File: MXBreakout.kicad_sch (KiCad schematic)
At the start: 16 parts, among them U1 Wii-MX, X1 32.768kHz

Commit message: initial changes
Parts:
- removed TP4: DATA0, TestPoint:TestPoint_Pad_D1.0mm, symbol Connector:TestPoint
- removed TP5: DATA1, TestPoint:TestPoint_Pad_D1.0mm, symbol Connector:TestPoint
- removed TP6: DATA2, TestPoint:TestPoint_Pad_D1.0mm, symbol Connector:TestPoint
- removed TP7: DATA3, TestPoint:TestPoint_Pad_D1.0mm, symbol Connector:TestPoint
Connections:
- net DATA3: now reaches U1.14 (DATA3)
- net DATA1: now reaches U1.12 (DATA1)
- net DATA2: now reaches U1.13 (DATA2)
- net DATA0: now reaches U1.11 (DATA0)
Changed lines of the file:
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@@
-    (stroke (width 0) (type default))
-  )
-  (wire (pts (xy 93.98 85.09) (xy 93.98 88.9))
     (stroke (width 0) (type default))
   )
@@
     (stroke (width 0) (type default))
   )
-  (wire (pts (xy 93.98 96.52) (xy 87.63 96.52))
-    (stroke (width 0) (type default))
-  )
-  (wire (pts (xy 93.98 90.17) (xy 93.98 91.44))
+  (wire (pts (xy 87.63 96.52) (xy 96.52 96.52))
     (stroke (width 0) (type default))
   )
@@
     (stroke (width 0) (type default))
   )
-  (wire (pts (xy 95.25 95.25) (xy 93.98 95.25))
-    (stroke (width 0) (type default))
-  )
   (wire (pts (xy 48.26 85.09) (xy 57.15 85.09))
     (stroke (width 0) (type default))
   )
-  (wire (pts (xy 93.98 88.9) (xy 87.63 88.9))
-    (stroke (width 0) (type default))
-  )
   (wire (pts (xy 30.48 85.09) (xy 30.48 88.9))
     (stroke (width 0) (type default))
   )
-  (wire (pts (xy 95.25 100.33) (xy 93.98 100.33))
-    (stroke (width 0) (type default))
-  )
   (wire (pts (xy 30.48 77.47) (xy 30.48 85.09))
     (stroke (width 0) (type default))
@@
     (stroke (width 0) (type default))
   )
+  (wire (pts (xy 87.63 91.44) (xy 96.52 91.44))
+    (stroke (width 0) (type default))
+  )
   (wire (pts (xy 106.68 78.74) (xy 104.14 78.74))
     (stroke (width 0) (type default))
@@
     (stroke (width 0) (type default))
   )
-  (wire (pts (xy 93.98 93.98) (xy 87.63 93.98))
-    (stroke (width 0) (type default))
-  )
   (wire (pts (xy 39.37 85.09) (xy 48.26 85.09))
     (stroke (width 0) (type default))
   )
-  (wire (pts (xy 95.25 90.17) (xy 93.98 90.17))
-    (stroke (width 0) (type default))
-  )
   (wire (pts (xy 57.15 80.01) (xy 57.15 77.47))
     (stroke (width 0) (type default))
   )
-  (wire (pts (xy 93.98 91.44) (xy 87.63 91.44))
-    (stroke (width 0) (type default))
-  )
   (wire (pts (xy 91.44 78.74) (xy 87.63 78.74))
     (stroke (width 0) (type default))
   )
-  (wire (pts (xy 93.98 95.25) (xy 93.98 93.98))
-    (stroke (width 0) (type default))
-  )
-  (wire (pts (xy 93.98 100.33) (xy 93.98 96.52))
-    (stroke (width 0) (type default))
-  )
-  (wire (pts (xy 93.98 85.09) (xy 95.25 85.09))
+  (wire (pts (xy 87.63 88.9) (xy 96.52 88.9))
+    (stroke (width 0) (type default))
+  )
+  (wire (pts (xy 87.63 93.98) (xy 96.52 93.98))
     (stroke (width 0) (type default))
   )
   (wire (pts (xy 43.18 81.28) (xy 43.18 86.36))
     (stroke (width 0) (type default))
+  )
+  (label "DATA1" (at 90.17 91.44 0) (fields_autoplaced)
+    (effects (font (size 1.27 1.27)) (justify left bottom))
+  )
+  (label "DATA2" (at 90.17 93.98 0) (fields_autoplaced)
+    (effects (font (size 1.27 1.27)) (justify left bottom))
+  )
+  (label "DATA0" (at 90.17 88.9 0) (fields_autoplaced)
+    (effects (font (size 1.27 1.27)) (justify left bottom))
+  )
+  (label "DATA3" (at 90.17 96.52 0) (fields_autoplaced)
+    (effects (font (size 1.27 1.27)) (justify left bottom))
   )
   (symbol (lib_id "power:GND") (at 30.48 88.9 0) (unit 1)
@@
     )
   )
-  (symbol (lib_id "Connector:TestPoint") (at 95.25 100.33 270) (unit 1)
-    (in_bom yes) (on_board yes) (dnp no) (fields_autoplaced)
-    (property "Reference" "TP7" (at 100.33 99.06 90)
-      (effects (font (size 1.27 1.27)) (justify left))
-    )
-    (property "Value" "DATA3" (at 100.33 101.6 90)
-      (effects (font (size 1.27 1.27)) (justify left))
-    )
-    (property "Footprint" "TestPoint:TestPoint_Pad_D1.0mm" (at 95.25 105.41 0)
-      (effects (font (size 1.27 1.27)) hide)
-    )
-    (property "Datasheet" "~" (at 95.25 105.41 0)
-      (effects (font (size 1.27 1.27)) hide)
-    )
-    (pin "1")
-    (instances
-      (project "MXBreakout"
-        (path "/b1683ed1-ed09-487c-8d86-af8ebf2f63f7"
-          (reference "TP7") (unit 1)
-        )
-      )
-    )
-  )
-  (symbol (lib_id "Connector:TestPoint") (at 95.25 90.17 270) (unit 1)
-    (in_bom yes) (on_board yes) (dnp no) (fields_autoplaced)
-    (property "Reference" "TP5" (at 100.33 88.9 90)
-      (effects (font (size 1.27 1.27)) (justify left))
-    )
-    (property "Value" "DATA1" (at 100.33 91.44 90)
-      (effects (font (size 1.27 1.27)) (justify left))
-    )
-    (property "Footprint" "TestPoint:TestPoint_Pad_D1.0mm" (at 95.25 95.25 0)
-      (effects (font (size 1.27 1.27)) hide)
-    )
-    (property "Datasheet" "~" (at 95.25 95.25 0)
-      (effects (font (size 1.27 1.27)) hide)
-    )
-    (pin "1")
-    (instances
-      (project "MXBreakout"
-        (path "/b1683ed1-ed09-487c-8d86-af8ebf2f63f7"
-          (reference "TP5") (unit 1)
-        )
-      )
-    )
-  )
   (symbol (lib_id "Device:C_Small") (at 36.83 77.47 90) (unit 1)
     (in_bom yes) (on_board yes) (dnp no) (fields_autoplaced)
@@
         (path "/b1683ed1-ed09-487c-8d86-af8ebf2f63f7"
           (reference "TP8") (unit 1)
-        )
-      )
-    )
-  )
-  (symbol (lib_id "Connector:TestPoint") (at 95.25 95.25 270) (unit 1)
-    (in_bom yes) (on_board yes) (dnp no) (fields_autoplaced)
-    (property "Reference" "TP6" (at 100.33 93.98 90)
-      (effects (font (size 1.27 1.27)) (justify left))
-    )
-    (property "Value" "DATA2" (at 100.33 96.52 90)
-      (effects (font (size 1.27 1.27)) (justify left))
-    )
-    (property "Footprint" "TestPoint:TestPoint_Pad_D1.0mm" (at 95.25 100.33 0)
-      (effects (font (size 1.27 1.27)) hide)
-    )
-    (property "Datasheet" "~" (at 95.25 100.33 0)
-      (effects (font (size 1.27 1.27)) hide)
-    )
-    (pin "1")
-    (instances
-      (project "MXBreakout"
-        (path "/b1683ed1-ed09-487c-8d86-af8ebf2f63f7"
-          (reference "TP6") (unit 1)
         )
       )
@@
         )
       )
-    )
-  )
-  (symbol (lib_id "Connector:TestPoint") (at 95.25 85.09 270) (unit 1)
-    (in_bom yes) (on_board yes) (dnp no)
-    (property "Reference" "TP4" (at 100.33 83.82 90)
-      (effects (font (size 1.27 1.27)) (justify left))
-    )
-    (property "Value" "DATA0" (at 100.33 86.36 90)
-      (effects (font (size 1.27 1.27)) (justify left))
-    )
-    (property "Footprint" "TestPoint:TestPoint_Pad_D1.0mm" (at 95.25 90.17 0)
-      (effects (font (size 1.27 1.27)) hide)
-    )
-    (property "Datasheet" "~" (at 95.25 90.17 0)
-      (effects (font (size 1.27 1.27)) hide)
-    )
-    (pin "1")
-    (instances
-      (project "MXBreakout"
-        (path "/b1683ed1-ed09-487c-8d86-af8ebf2f63f7"
-          (reference "TP4") (unit 1)
-        )
-      )

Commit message: nearing completion
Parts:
- removed TP1: BATT, TestPoint:TestPoint_Pad_D4.0mm, symbol Connector:TestPoint
- added TP10: TestPoint_2Pole, Resistor_SMD:R_0402_1005Metric, symbol Connector:TestPoint_2Pole
- added TP11: U10, Wii:TestPoint_THTPad_D0.5mm_Drill0.35mm, symbol Connector:TestPoint
- added TP4, TP5, TP6, TP7: TestPoint, Wii:TestPoint_THTPad_D0.5mm_Drill0.35mm, symbol Connector:TestPoint
- added U10: ~, Package_TO_SOT_SMD:SOT-23-5, symbol Wii:U10
- TP2: footprint TestPoint:TestPoint_Pad_D4.0mm -> TestPoint:TestPoint_Pad_D1.0mm
- TP3: footprint TestPoint:TestPoint_Pad_D1.0mm -> Wii:TestPoint_THTPad_D0.5mm_Drill0.35mm
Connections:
- net +3.3V: now also TP10.1, TP10.2, U10.5 (3.3V)
- net DATA0: now also TP4.1
- net DATA1: now also TP5.1
- net DATA2: now also TP6.1
- net DATA3: now also TP7.1
- net GND: now also U10.1 (GND), U10.2 (GND), U10.3 (GND)
- new net: TP11.1, U10.4 (RST)
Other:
- moved on the sheet: TP2, TP3

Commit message: HopefullyFinal
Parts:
- removed TP10: TestPoint_2Pole, Resistor_SMD:R_0402_1005Metric, symbol Connector:TestPoint_2Pole
- removed TP2: GND, TestPoint:TestPoint_Pad_D1.0mm, symbol Connector:TestPoint
- removed X1: 32.768kHz, Crystal:Crystal_SMD_Abracon_ABS25-4Pin_8.0x3.8mm, symbol Device:Crystal_GND23
- added TP12: U10, TestPoint:TestPoint_Pad_D1.0mm, symbol Connector:TestPoint
- added Y1: 32.768kHz, Crystal:Crystal_SMD_2012-2Pin_2.0x1.2mm, symbol Device:Crystal
- C1, C2: MouserPart (none) -> 81-GRM1555C1H5R0BA1D
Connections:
- net at TP11.1, U10.4 (RST): now also TP12.1
- net at C2.2, U1.22 (X_2): now also Y1.1
- net at C1.2, U1.23 (X_1): now also Y1.2
- net BATT: now reaches R1.2, TP8.1

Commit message: Minor cleanup
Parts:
- removed TP11: U10, Wii:TestPoint_THTPad_D0.5mm_Drill0.35mm, symbol Connector:TestPoint
- removed TP12: U10, TestPoint:TestPoint_Pad_D1.0mm, symbol Connector:TestPoint
- removed U10: ~, Package_TO_SOT_SMD:SOT-23-5, symbol Wii:U10
- added TP1: BATT, TestPoint:TestPoint_Pad_D1.0mm, symbol Connector:TestPoint
- added TP2: DATA0, Wii:TestPoint_THTPad_D0.5mm_Drill0.35mm, symbol Connector:TestPoint
- added U2: ~, Package_TO_SOT_SMD:SOT-23-5, symbol Wii:U10
- TP3: value GND -> DATA1
- TP4: value TestPoint -> DATA2
- TP5: value TestPoint -> DATA3
- TP6: value TestPoint -> U10; footprint Wii:TestPoint_THTPad_D0.5mm_Drill0.35mm -> TestPoint:TestPoint_Pad_D1.0mm
- TP7: value TestPoint -> U10
- TP8: value BATT -> 3.3V
- TP9: value 3.3V -> GND; footprint TestPoint:TestPoint_Pad_D1.0mm -> Wii:TestPoint_THTPad_D0.5mm_Drill0.35mm
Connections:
- net +3.3V: now also TP8.1, U2.5 (3.3V); no longer TP9.1
- net BATT: now also TP1.1; no longer TP8.1
- net DATA0: now also TP2.1; no longer TP4.1
- net DATA1: now also TP3.1; no longer TP5.1
- net DATA2: now also TP4.1; no longer TP6.1
- net DATA3: now also TP5.1; no longer TP7.1
- net GND: now also TP9.1, U2.1 (GND), U2.2 (GND), U2.3 (GND); no longer TP3.1
- new net: TP6.1, TP7.1, U2.4 (RST)

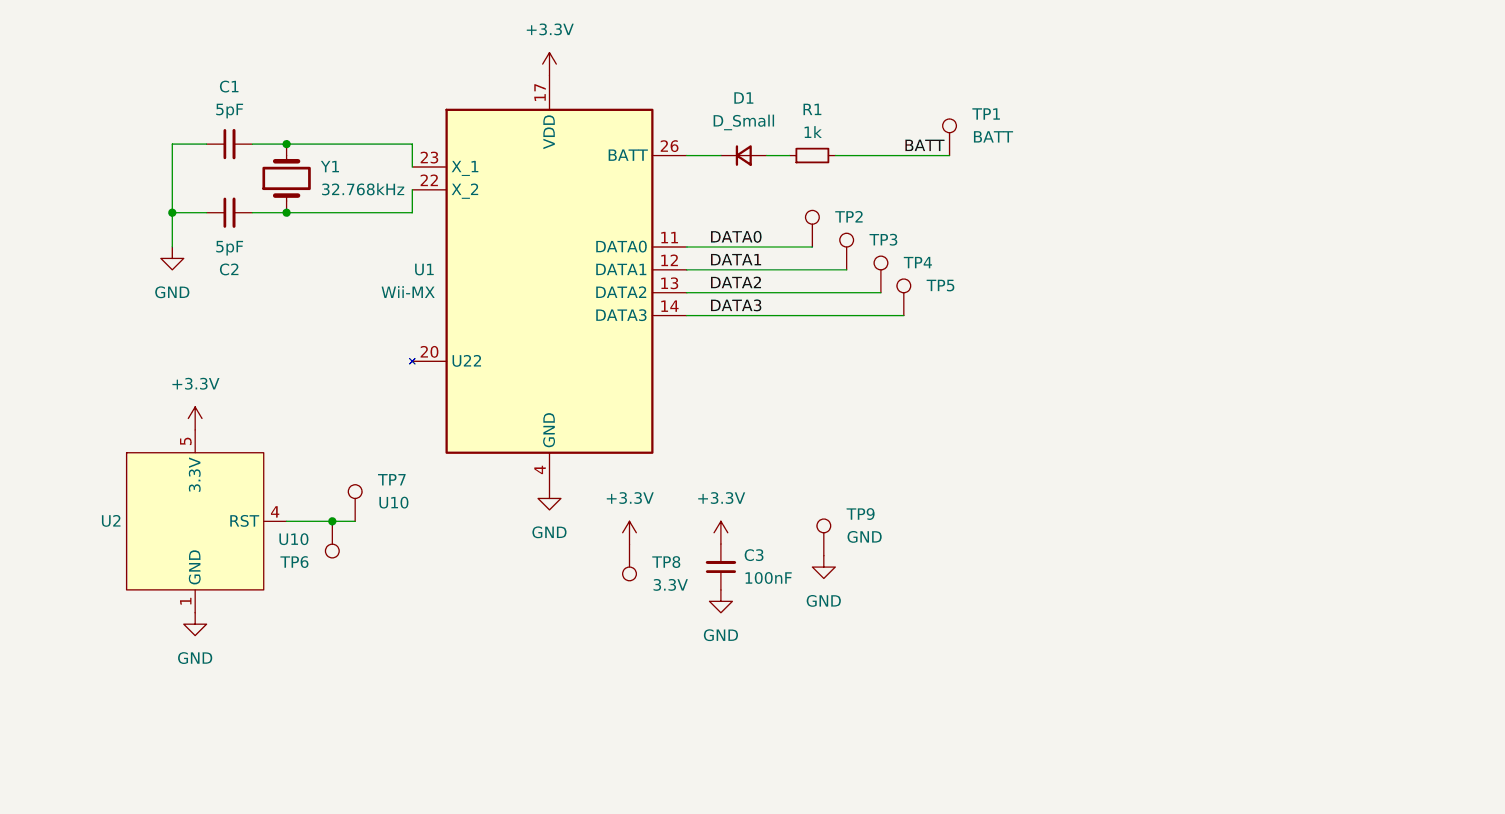
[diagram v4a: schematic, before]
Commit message: Fix pad alignment, add soft shutdown
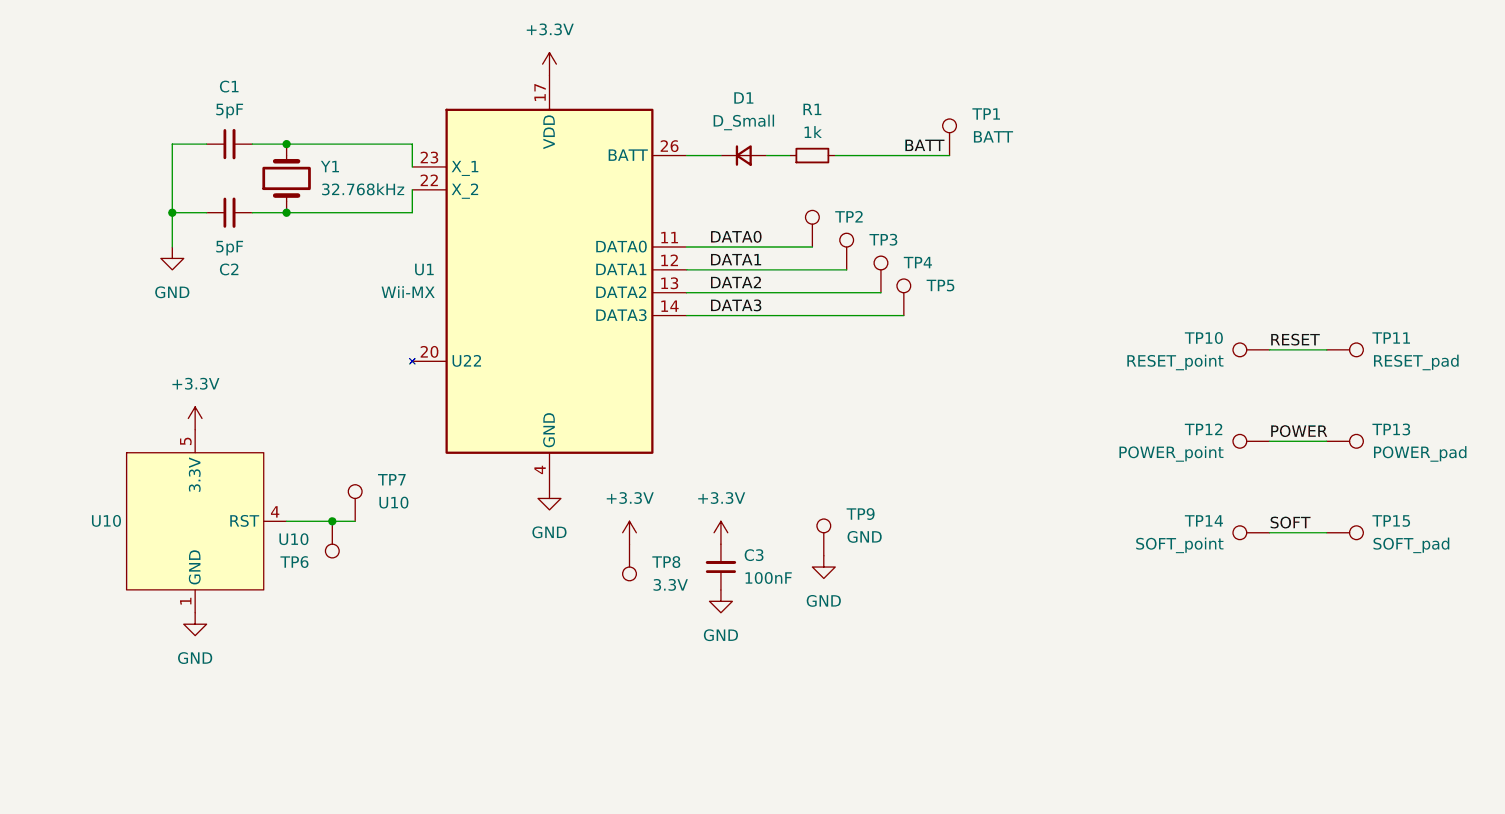
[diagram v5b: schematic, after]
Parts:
- added TP10: RESET_point, Wii:TestPoint_THTPad_D0.5mm_Drill0.35mm, symbol Connector:TestPoint
- added TP11: RESET_pad, Wii:TestPoint_Pad_D0.5mm, symbol Connector:TestPoint
- added TP12: POWER_point, Wii:TestPoint_THTPad_D0.5mm_Drill0.35mm, symbol Connector:TestPoint
- added TP13: POWER_pad, Wii:TestPoint_Pad_D0.5mm, symbol Connector:TestPoint
- added TP14: SOFT_point, Wii:TestPoint_THTPad_D0.5mm_Drill0.35mm, symbol Connector:TestPoint
- added TP15: SOFT_pad, Wii:TestPoint_Pad_D0.5mm, symbol Connector:TestPoint
- TP6: footprint TestPoint:TestPoint_Pad_D1.0mm -> Wii:TestPoint_Pad_D0.5mm
- U1: footprint Package_SO:SOIC-28W_7.5x17.9mm_P1.27mm -> Wii:MX_SOIC
- renumbered U2 to U10
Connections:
- new net POWER: TP12.1, TP13.1
- new net RESET: TP10.1, TP11.1
- new net SOFT: TP14.1, TP15.1

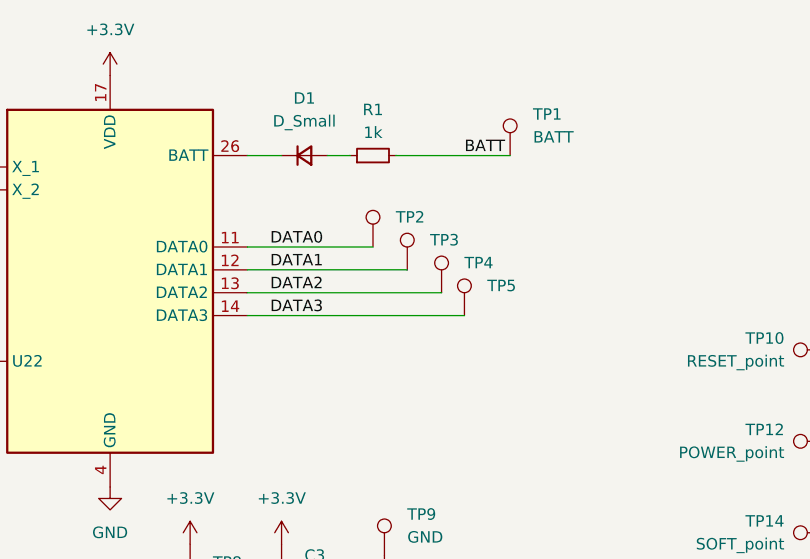
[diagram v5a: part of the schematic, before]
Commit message: Add pads for EXI bus, primarily for RVL-DD
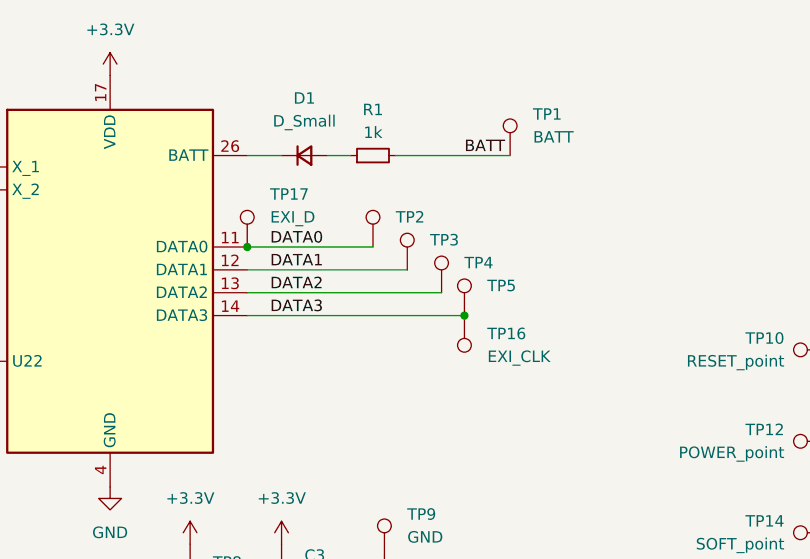
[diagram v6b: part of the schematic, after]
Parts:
- added TP16: EXI_CLK, Wii:TestPoint_Pad_D0.5mm, symbol Connector:TestPoint
- added TP17: EXI_D, Wii:TestPoint_Pad_D0.5mm, symbol Connector:TestPoint
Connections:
- net DATA0: now also TP17.1
- net DATA3: now also TP16.1
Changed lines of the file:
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@@
 (kicad_sch
-	(version 20240101)
+	(version 20240417)
 	(generator "eeschema")
 	(generator_version "8.99")
@@
 	)
 	(junction
+		(at 114.3 93.98)
+		(diameter 0)
+		(color 0 0 0 0)
+	)
+	(junction
+		(at 90.17 86.36)
+		(diameter 0)
+		(color 0 0 0 0)
+	)
+	(junction
 		(at 33.02 82.55)
 		(diameter 0)
@@
 	)
 	(symbol
+		(lib_id "Connector:TestPoint")
+		(at 114.3 93.98 180)
+		(unit 1)
+		(exclude_from_sim no)
+		(in_bom yes)
+		(on_board yes)
+		(dnp no)
+		(fields_autoplaced yes)
+		(property "Reference" "TP16"
+			(at 116.84 96.0119 0)
+			(effects
+				(font
+					(size 1.27 1.27)
+				)
+				(justify right)
+			)
+		)
+		(property "Value" "EXI_CLK"
+			(at 116.84 98.5519 0)
+			(effects
+				(font
+					(size 1.27 1.27)
+				)
+				(justify right)
+			)
+		)
+		(property "Footprint" "Wii:TestPoint_Pad_D0.5mm"
+			(at 109.22 93.98 0)
+			(effects
+				(font
+					(size 1.27 1.27)
+				)
+				(hide yes)
+			)
+		)
+		(property "Datasheet" "~"
+			(at 109.22 93.98 0)
+			(effects
+				(font
+					(size 1.27 1.27)
+				)
+				(hide yes)
+			)
+		)
+		(property "Description" "test point"
+			(at 114.3 93.98 0)
+			(effects
+				(font
+					(size 1.27 1.27)
+				)
+				(hide yes)
+			)
+		)
+		(pin "1"
+		)
+		(instances
+			(project "MXBreakout"
+				(path "/b1683ed1-ed09-487c-8d86-af8ebf2f63f7"
+					(reference "TP16")
+					(unit 1)
+				)
+			)
+		)
+	)
+	(symbol
 		(lib_id "power:+3.3V")
 		(at 83.82 119.38 0)
@@
 					(unit 1)
 				)
+			)
+		)
+	)
+	(symbol
+		(lib_id "Connector:TestPoint")
+		(at 90.17 86.36 0)
+		(unit 1)
+		(exclude_from_sim no)
+		(in_bom yes)
+		(on_board yes)
+		(dnp no)
+		(property "Reference" "TP17"
+			(at 92.71 80.518 0)
+			(effects
+				(font
+					(size 1.27 1.27)
+				)
+				(justify left)
+			)
+		)
+		(property "Value" "EXI_D"
+			(at 92.71 83.058 0)
+			(effects
+				(font
+					(size 1.27 1.27)
+				)
+				(justify left)
+			)
+		)
+		(property "Footprint" "Wii:TestPoint_Pad_D0.5mm"
+			(at 95.25 86.36 0)
+			(effects
+				(font
+					(size 1.27 1.27)
+				)
+				(hide yes)
+			)
+		)
+		(property "Datasheet" "~"
+			(at 95.25 86.36 0)
+			(effects
+				(font
+					(size 1.27 1.27)
+				)
+				(hide yes)
+			)
+		)
+		(property "Description" "test point"
+			(at 90.17 86.36 0)
+			(effects
+				(font
+					(size 1.27 1.27)
+				)
+				(hide yes)
+			)
+		)
+		(pin "1"
+		)
+		(instances
+			(project "MXBreakout"
+				(path "/b1683ed1-ed09-487c-8d86-af8ebf2f63f7"
+					(reference "TP17")
+					(unit 1)
+				)

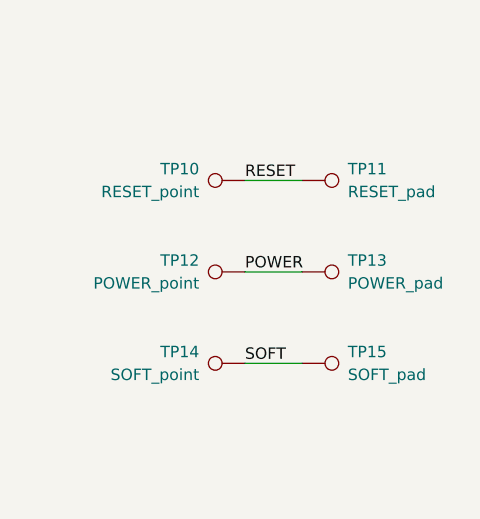
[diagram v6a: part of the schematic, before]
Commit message: Clean up PCB, regenerate gerbers
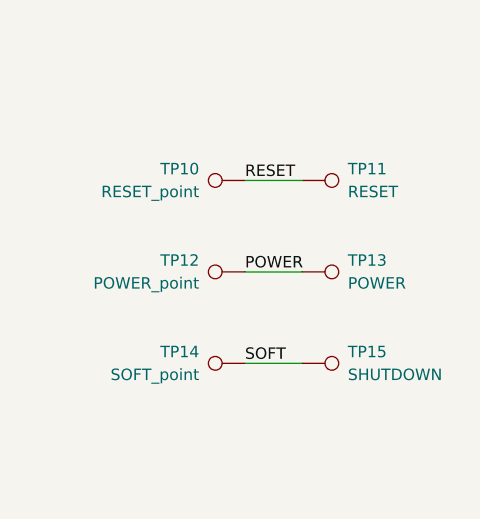
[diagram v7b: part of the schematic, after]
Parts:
- TP11: value RESET_pad -> RESET
- TP13: value POWER_pad -> POWER
- TP15: value SOFT_pad -> SHUTDOWN
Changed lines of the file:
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@@
 			)
 		)
-		(property "Value" "SOFT_pad"
+		(property "Value" "SHUTDOWN"
 			(at 166.37 119.3799 90)
 			(effects
@@
 			)
 		)
-		(property "Value" "POWER_pad"
+		(property "Value" "POWER"
 			(at 166.37 109.2199 90)
 			(effects
@@
 			)
 		)
-		(property "Value" "RESET_pad"
+		(property "Value" "RESET"
 			(at 166.37 99.0599 90)
 			(effects
